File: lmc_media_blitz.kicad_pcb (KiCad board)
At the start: 2 copper layers, 76.2 x 114.3 mm, 69 parts, among them Q1 BSS138, Q2 BSS138, U1 TPS61222DCK, U10 SK9822, U11 SK9822, U12 SK9822, U13 SK9822, U14 SK9822, U2 TLV77333PDBVR, U3 LPC804M101JDH20, U4 ST25R3918AQW, Y1 27.12MHz

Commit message: Adding some stuf
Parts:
- removed the C10 at (128.3, 75.6)
- removed the C10 at (173.4, 86.2)
- removed the C11 at (173.4, 89.2)
- removed the C11 at (128.3, 78.6)
- removed the C12 at (173.4, 92.2)
- removed the C12 at (128.3, 81.6)
- removed the C13 at (128.3, 84.6)
- removed the C13 at (173.4, 95.2)
- removed the C14 at (128.3, 87.6)
- removed the C14 at (177.8, 80.2)
- removed the C15 at (156.8, 110.5)
- removed the C15 at (132.8, 69.6)
- removed the C16 at (157.0, 104.8)
- removed the C16 at (132.8, 72.6)
- removed the C17 at (132.8, 75.6)
- removed the C17 at (177.8, 83.2)
- removed the C18 at (177.8, 86.2)
- removed the C18 at (132.8, 78.6)
- removed the C19 at (177.8, 89.2)
- removed the C19 at (132.8, 81.6)
- removed the C20 at (132.8, 84.6)
- removed the C20 at (177.8, 92.2)
- removed the C21 at (132.8, 87.6)
- removed the C21 at (177.8, 95.2)
- removed the C22 at (137.2, 69.6)
- removed the C22 at (182.3, 80.2)
- removed the C23 at (182.3, 83.2)
- removed the C23 at (137.2, 72.6)
- removed the C24 at (137.2, 75.6)
- removed the C24 at (182.3, 86.2)
- removed the C25 at (141.5, 87.0)
- removed the C25 at (182.3, 89.2)
- removed the C26 at (182.3, 92.2)
- removed the C26 at (141.5, 89.5)
- removed the C8 at (128.3, 69.6)
- removed the C8 at (173.4, 80.2)
- removed the C9 at (128.3, 72.6)
- removed the C9 at (173.4, 83.2)
- added AE1: Antenna_Loop, footprints:badge_antenna, F.Cu at (178.0, 150.9)
- added C10: 1uF, Capacitor_SMD:C_0603_1608Metric, F.Cu at (151.4, 96.0)
- added C11: 10nF, Capacitor_SMD:C_0603_1608Metric, F.Cu at (145.8, 109.7)
- added C12: 10nF, Capacitor_SMD:C_0603_1608Metric, F.Cu at (147.3, 109.7)
- added C13: 10nF, Capacitor_SMD:C_0603_1608Metric, F.Cu at (149.9, 96.0)
- added C14: 1uF, Capacitor_SMD:C_0603_1608Metric, F.Cu at (158.0, 98.0)
- added C15: 15pF, Capacitor_SMD:C_0603_1608Metric, F.Cu at (143.0, 101.9)
- added C16: 15pF, Capacitor_SMD:C_0603_1608Metric, F.Cu at (145.5, 99.1)
- added C17: 10nF, Capacitor_SMD:C_0603_1608Metric, F.Cu at (158.0, 99.6)
- added C18: 10nF, Capacitor_SMD:C_0603_1608Metric, F.Cu at (145.0, 104.4)
- added C19: 10nF, Capacitor_SMD:C_0603_1608Metric, F.Cu at (148.3, 96.0)
- added C20: 10nF, Capacitor_SMD:C_0603_1608Metric, F.Cu at (145.8, 106.7)
- added C21: 2.2uF, Capacitor_SMD:C_0603_1608Metric, F.Cu at (142.7, 106.7)
- added C22: 2.2uF, Capacitor_SMD:C_0603_1608Metric, F.Cu at (146.8, 96.0)
- added C23: 2.2uF, Capacitor_SMD:C_0603_1608Metric, F.Cu at (147.8, 106.7)
- added C24: 1nF, Capacitor_SMD:C_0603_1608Metric, F.Cu at (150.9, 106.7)
- added C25: 10nF, Capacitor_SMD:C_0603_1608Metric, F.Cu at (149.4, 106.7)
- added C26: 2.2uF, Capacitor_SMD:C_0603_1608Metric, F.Cu at (144.3, 106.7)
- added C32: 22nF, Capacitor_SMD:C_0805_2012Metric, F.Cu at (91.1, 97.5)
- added C33: C, Capacitor_SMD:C_0805_2012Metric, F.Cu at (151.6, 110.0)
- added C34: C, Capacitor_SMD:C_0805_2012Metric, F.Cu at (155.2, 110.0)
- added C35: C, Capacitor_SMD:C_0805_2012Metric, F.Cu at (152.4, 113.0)
- added C36: C, Capacitor_SMD:C_0805_2012Metric, F.Cu at (154.4, 113.0)
- added C37: C, Capacitor_SMD:C_0805_2012Metric, F.Cu at (150.4, 113.0)
- added C38: C, Capacitor_SMD:C_0805_2012Metric, F.Cu at (156.5, 113.0)
- added C39: C, Capacitor_SMD:C_0805_2012Metric, F.Cu at (149.6, 115.8)
- added C40: C, Capacitor_SMD:C_0805_2012Metric, F.Cu at (148.3, 113.0)
- added C41: C, Capacitor_SMD:C_0805_2012Metric, F.Cu at (158.5, 113.0)
- added C42: C, Capacitor_SMD:C_0805_2012Metric, F.Cu at (157.2, 115.8)
- added C8: 1uF, Capacitor_SMD:C_0603_1608Metric, F.Cu at (144.3, 109.7)
- added C9: 1uF, Capacitor_SMD:C_0603_1608Metric, F.Cu at (148.8, 109.7)
- added J1: Conn_ARM_JTAG_SWD_10, Capacitor_SMD:C_0805_2012Metric, F.Cu at (104.8, 77.5)
- added J2: ~, footprints:Keystone82, F.Cu at (130.9, 62.0)
- added J3: ~, footprints:Keystone82, F.Cu at (173.9, 62.0)
- added L2: 270nH, Inductor_SMD:L_0805_2012Metric, F.Cu at (152.7, 107.2)
- added L3: 270nH, Inductor_SMD:L_0805_2012Metric, F.Cu at (154.4, 107.2)
- added R7: R, Resistor_SMD:R_0805_2012Metric, F.Cu at (152.4, 116.6)
- added R8: R, Resistor_SMD:R_0805_2012Metric, F.Cu at (154.4, 116.6)
- added TP1: TestPoint_Small, TestPoint:TestPoint_Pad_D2.0mm, F.Cu at (78.5, 95.8)
- added TP2: TestPoint_Small, TestPoint:TestPoint_Pad_D2.0mm, F.Cu at (78.7, 91.4)
- U4: footprint Package_DFN_QFN:VQFN-32-1EP_5x5mm_P0.5mm_EP3.1x3.1mm -> Package_DFN_QFN:HVQFN-32-1EP_5x5mm_P0.5mm_EP3.1x3.1mm
- moved L1 58.8 mm to (99.5, 85.5)
- moved Q1 58.8 mm to (97.0, 94.1)
- moved R1 58.8 mm to (84.8, 84.5)
- moved R2 58.8 mm to (84.8, 87.5)
- moved R3 58.8 mm to (84.8, 90.4)
- moved R4 58.8 mm to (84.8, 93.4)
- moved R5 58.8 mm to (84.8, 96.3)
- moved R6 58.8 mm to (84.8, 99.3)
- moved U2 58.5 mm to (131.6, 73.2)
- moved Q2 58.4 mm to (105.9, 90.9)
- moved U1 58.4 mm to (107.3, 86.1)
- moved U3 44.4 mm to (93.0, 84.8)
- moved C1 28.9 mm to (97.5, 57.6)
- moved C7 28.9 mm to (97.5, 75.7)
- moved C3 28.9 mm to (97.5, 63.7)
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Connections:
- U3 pad 1: unconnected-(U3-PIO0_16/ADC_3/ACMP_I4-Pad1) -> /CAPT_X0
- U3 pad 19: unconnected-(U3-PIO0_0/ACMP_I1/TDO-Pad19) -> /ACMP_I1
- U3 pad 3: unconnected-(U3-PIO0_13/ADC_10-Pad3) -> /CAPT_X1
- U3 pad 4: unconnected-(U3-PIO0_12-Pad4) -> /CAPT_X2
- U3 pad 6: unconnected-(U3-PIO0_4/ADC_11/~{TRST}-Pad6) -> /CAPT_YL
- U3 pad 9: unconnected-(U3-PIO0_11/ADC_6/WKTCLKIN-Pad9) -> /ACMP_I1
- U4 pad 13: unconnected-(U4-RFO1-Pad13) -> Net-(U4-RFO1)
- U4 pad 15: unconnected-(U4-RFO2-Pad15) -> Net-(U4-RFO2)
- U4 pad 22: unconnected-(U4-RFI1-Pad22) -> Net-(U4-RFI1)
- U4 pad 23: unconnected-(U4-RFI2-Pad23) -> Net-(U4-RFI2)
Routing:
- net Net-(U4-RFI1): track 0.00 -> 37.6 mm, vias 0 -> 4
- net Net-(U4-RFI2): track 0.00 -> 17.7 mm
- net Net-(AE1-Pad2): track 0.00 -> 11.4 mm, vias 0 -> 2
- net +5V: track 0.00 -> 9.85 mm
- net Net-(U4-VDD_A): track 0.00 -> 9.61 mm
- net Net-(U4-XTI): track 0.00 -> 8.09 mm
- net Net-(U4-VDD_DR): track 0.00 -> 7.07 mm
- net Net-(U4-XTO): track 0.00 -> 5.07 mm
- net Net-(U4-VDD_AM): track 0.00 -> 4.92 mm
- net Net-(C36-Pad2): track 0.00 -> 4.51 mm
- net Net-(C35-Pad2): track 0.00 -> 4.51 mm
- net Net-(AE1-Pad1): track 0.00 -> 4.36 mm
- net Net-(C34-Pad2): track 0.00 -> 3.99 mm
- net Net-(C33-Pad1): track 0.00 -> 3.93 mm
- net Net-(U4-RFO2): track 0.00 -> 2.21 mm
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
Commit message: WIP
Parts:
- added TP3: TestPoint_Small, TestPoint:TestPoint_Pad_D2.0mm, F.Cu at (135.1, 73.2)
- added TP4: TestPoint_Small, TestPoint:TestPoint_Pad_D2.0mm, F.Cu at (151.4, 73.2)
- C5, C6: footprint Capacitor_SMD:C_0805_2012Metric -> Capacitor_SMD:C_0603_1608Metric
- moved C7 63.4 mm to (160.0, 86.4), turned to 90 degrees
- moved C5 62.7 mm to (158.0, 86.4), turned to -90 degrees
- moved C6 60.5 mm to (156.5, 86.4), turned to -90 degrees
- moved U3 56.4 mm to (149.4, 85.3)
- moved R1 53.4 mm to (138.2, 86.0)
- moved R2 53.4 mm to (138.2, 88.9)
- moved C4 50.3 mm to (147.3, 74.2), turned to -90 degrees
- moved C3 43.9 mm to (140.2, 74.2), turned to -90 degrees
- moved C2 35.2 mm to (130.0, 74.2), turned to 90 degrees
- moved C1 32.0 mm to (125.0, 74.2), turned to 90 degrees
- moved L1 30.8 mm to (126.5, 70.6)
- moved U1 23.5 mm to (127.5, 74.2), turned to 90 degrees
- moved U2 12.2 mm to (143.8, 74.2)
- moved U14 10.1 mm to (127.0, 54.9), turned to 180 degrees
- moved U10 9.18 mm to (177.8, 54.9), turned to 180 degrees
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- renumbered J2 to J1, J3 to J2, J1 to J3
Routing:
- net +5V: track 9.85 -> 102.3 mm
- net +3V3: track 0.00 -> 31.2 mm
- net +BATT: track 0.00 -> 26.6 mm
- net GND: track 0.00 -> 15.1 mm, vias 0 -> 10
- net Net-(U1-L): track 0.00 -> 2.49 mm
- added copper zone on B.Cu, net GND

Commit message: WIP
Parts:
- added G***: LOGO, footprints:badge_silk, B.Cu at (152.4, 95.5)
- added REF**: Keystone82Spacer, footprints:Keystone82Spacer, F.Cu at (152.4, 62.5)
- added S1: ~, footprints:CapTouchButton, B.Cu at (185.7, 82.6)
- added S2: ~, footprints:CapTouchButton, B.Cu at (185.7, 99.4)
- added S3: ~, footprints:CapTouchButton, B.Cu at (185.7, 115.1)
- J3: footprint Capacitor_SMD:C_0805_2012Metric -> Connector_PinHeader_1.27mm:PinHeader_2x05_P1.27mm_Vertical_SMD
- moved R4 86.8 mm to (169.7, 75.2), turned to -90 degrees
- moved R3 84.3 mm to (167.6, 75.2), turned to -90 degrees
- moved R6 82.4 mm to (163.6, 75.2), turned to -90 degrees
- moved R5 79.6 mm to (161.5, 75.2), turned to -90 degrees
- moved Q1 73.2 mm to (168.7, 79.2)
- moved TP1 59.6 mm to (135.1, 77.2)
- moved Q2 57.8 mm to (162.6, 79.2)
- moved TP2 57.3 mm to (135.1, 81.3)
- moved C32 54.5 mm to (145.3, 91.9), turned to 90 degrees
- moved C31 36.8 mm to (127.0, 57.9), turned to 0 degrees
- moved J3 34.2 mm to (137.2, 88.4)
- moved C30 29.7 mm to (139.7, 57.9), turned to 0 degrees
- moved C29 21.9 mm to (152.4, 57.9), turned to 0 degrees
- moved C28 14.6 mm to (165.1, 57.9), turned to 0 degrees
- moved C27 10.3 mm to (177.8, 57.9), turned to 0 degrees
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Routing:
- net +5V: track 102.3 -> 232.6 mm, vias 0 -> 5
- net +3V3: track 31.2 -> 70.5 mm, vias 0 -> 2
- net /LEDs/CKI: track 0.00 -> 38.8 mm, vias 0 -> 1
- net /LEDs/SDI: track 0.00 -> 36.3 mm, vias 0 -> 1
- net /SPI0_MOSI: track 0.00 -> 23.1 mm
- net /SPI0_SCKB: track 0.00 -> 14.5 mm, vias 0 -> 2
- net GND: track 15.1 -> 28.3 mm, vias 10 -> 19
- net /MCU_CLK: track 0.00 -> 13.1 mm
- net Net-(J3-~{RESET}): track 0.00 -> 12.7 mm, vias 0 -> 2
- net /CAPT_X2: track 0.00 -> 12.6 mm
- net Net-(J3-SWCLK/TCK): track 0.00 -> 11.0 mm, vias 0 -> 2
- net Net-(J3-SWDIO/TMS): track 0.00 -> 10.0 mm
- net Net-(U13-SDO): track 0.00 -> 7.50 mm
- net Net-(U13-CKO): track 0.00 -> 7.50 mm
- net Net-(U12-SDO): track 0.00 -> 7.50 mm
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
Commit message: Initial routing
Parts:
- moved C32 26.8 mm to (172.0, 93.6), turned to 180 degrees
- moved C21 3.42 mm to (140.5, 104.1), turned to 0 degrees
- moved C11 3.39 mm to (144.5, 106.6)
- moved C8 3.38 mm to (143.0, 106.6)
- moved C23 2.94 mm to (147.5, 109.6)
- moved C9 2.85 mm to (146.0, 109.6)
- moved C12 2.82 mm to (144.5, 109.6)
- moved C25 1.95 mm to (149.0, 108.6)
- moved C20 1.80 mm to (147.5, 106.1)
- moved C26 1.73 mm to (146.0, 106.6)
- moved C18 1.56 mm to (143.5, 104.1)
- moved TP2 1.32 mm to (135.1, 82.6)
- moved C15 0.74 mm to (142.5, 101.3)
- moved C16 0.74 mm to (145.0, 98.6)
- moved Y1 0.74 mm to (145.5, 101.1)
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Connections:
- C32 pad 1: /ACMP_I1 -> /ACMP_I4
- S1 pad 2: /ACMP_I1 -> /ACMP_I4
- S2 pad 2: /ACMP_I1 -> /ACMP_I4
- S3 pad 2: /ACMP_I1 -> /ACMP_I4
- TP2 pad 1: /CAPT_X2 -> /CAPT_X1
- U3 pad 1: /CAPT_X0 -> /ACMP_I4
- U3 pad 19: /ACMP_I1 -> /CAPT_YL
- U3 pad 2: /NFC_IRQ -> /ACMP_I4
- U3 pad 3: /CAPT_X1 -> /CAPT_X0
- U3 pad 4: /CAPT_X2 -> /CAPT_X1
- U3 pad 6: /CAPT_YL -> /CAPT_X2
- U3 pad 9: /ACMP_I1 -> /NFC_IRQ
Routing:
- net /ACMP_I4: track 0.00 -> 73.6 mm, vias 0 -> 7
- net /CAPT_X1: track 0.00 -> 57.0 mm, vias 0 -> 3
- net +3V3: track 70.5 -> 118.9 mm, vias 2 -> 0
- net /CAPT_X2: track 12.6 -> 60.3 mm, vias 0 -> 3
- net GND: track 28.3 -> 67.0 mm, vias 19 -> 52
- net /CAPT_X0: track 0.00 -> 34.9 mm, vias 0 -> 5
- net /CAPT_YL: track 0.00 -> 28.1 mm, vias 0 -> 4
- net /SPI0_MOSI: track 23.1 -> 41.8 mm
- net /NFC_IRQ: track 0.00 -> 18.6 mm, vias 0 -> 2
- net /SPI0_SSEL0: track 0.00 -> 14.9 mm, vias 0 -> 2
- net /SPI0_MISO: track 0.00 -> 14.2 mm
- net /SPI0_SCKA: track 0.00 -> 11.5 mm
- net Net-(U4-VDD_D): track 0.00 -> 6.27 mm
- net +5V: track 232.6 -> 235.2 mm
- net Net-(C36-Pad2): track 4.51 -> 6.54 mm
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
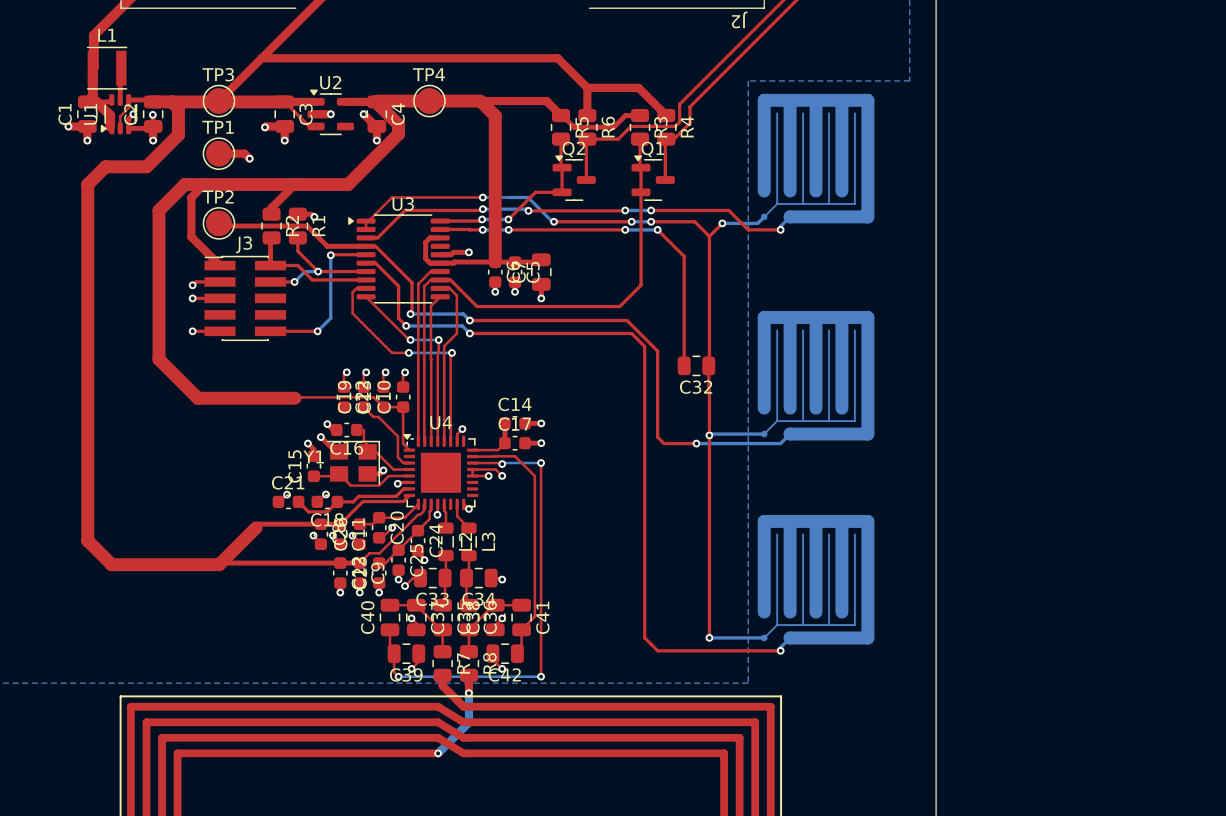
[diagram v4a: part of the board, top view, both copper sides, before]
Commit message: Fixed most DRC errors, but need to relayout RFO/RFI
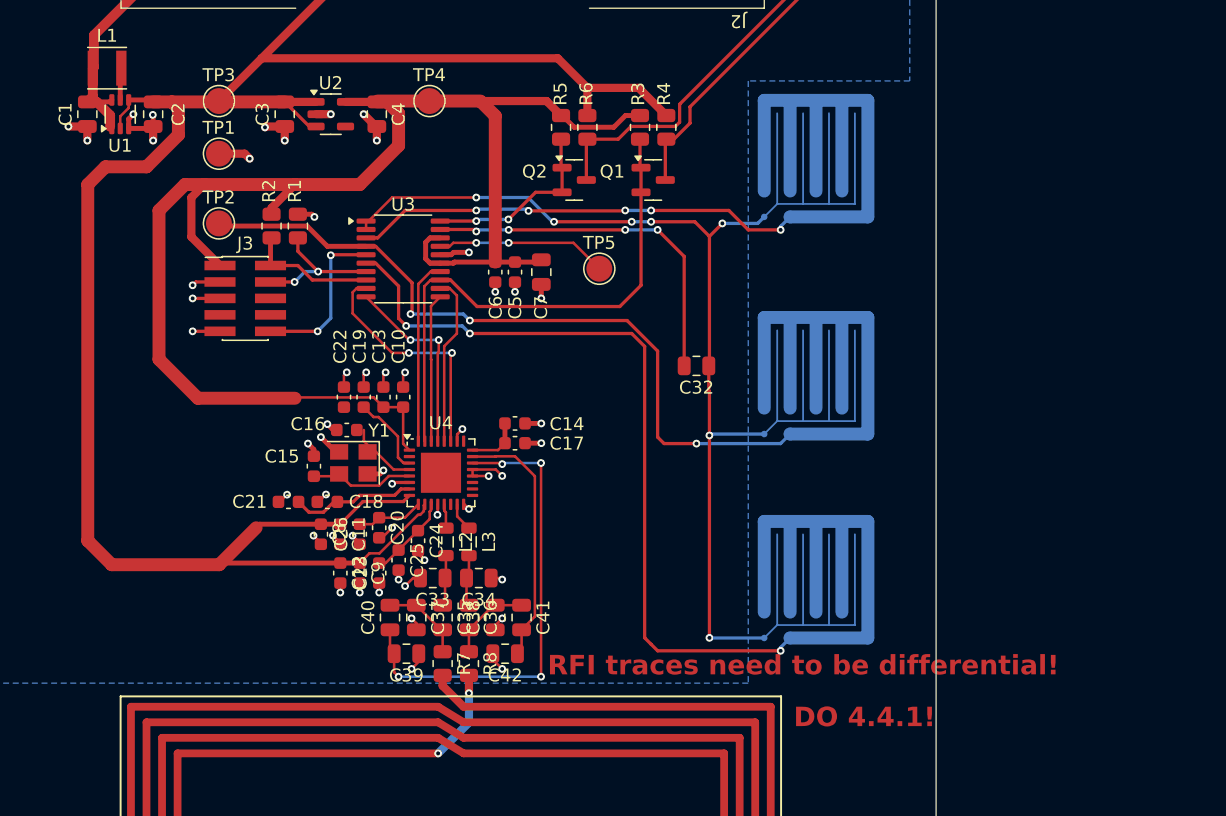
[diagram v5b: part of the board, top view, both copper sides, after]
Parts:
- added TP5: TestPoint_Small, TestPoint:TestPoint_Pad_D2.0mm, F.Cu at (164.5, 86.1)
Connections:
- net /ACMP_I4 renamed /CAPT_YH
- U3 pad 17: unconnected-(U3-PIO0_7/ADC_1/ACMPV_{REF}-Pad17) -> Net-(U3-PIO0_7/ADC_1/ACMPV_{REF})
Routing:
- net Net-(U3-PIO0_7/ADC_1/ACMPV_{REF}): track 0.00 -> 13.2 mm, vias 0 -> 2
- net +3V3: track 118.9 -> 119.8 mm
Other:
- board text added: "DO 4.4.1!"
- board text added: "RFI traces need to be differential!"
